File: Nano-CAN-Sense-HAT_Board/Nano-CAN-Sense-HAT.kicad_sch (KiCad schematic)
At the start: 33 parts, among them J1 Analog, J2 Digital, J3 Conn_02x04_Counter_Clockwise, J4 Conn_02x04_Counter_Clockwise, J5 Conn_01x05, J6 Conn_01x03, SW1 SW_Push, SW2 SW_Push, U1 LMC6484, U4 TCAN1044A

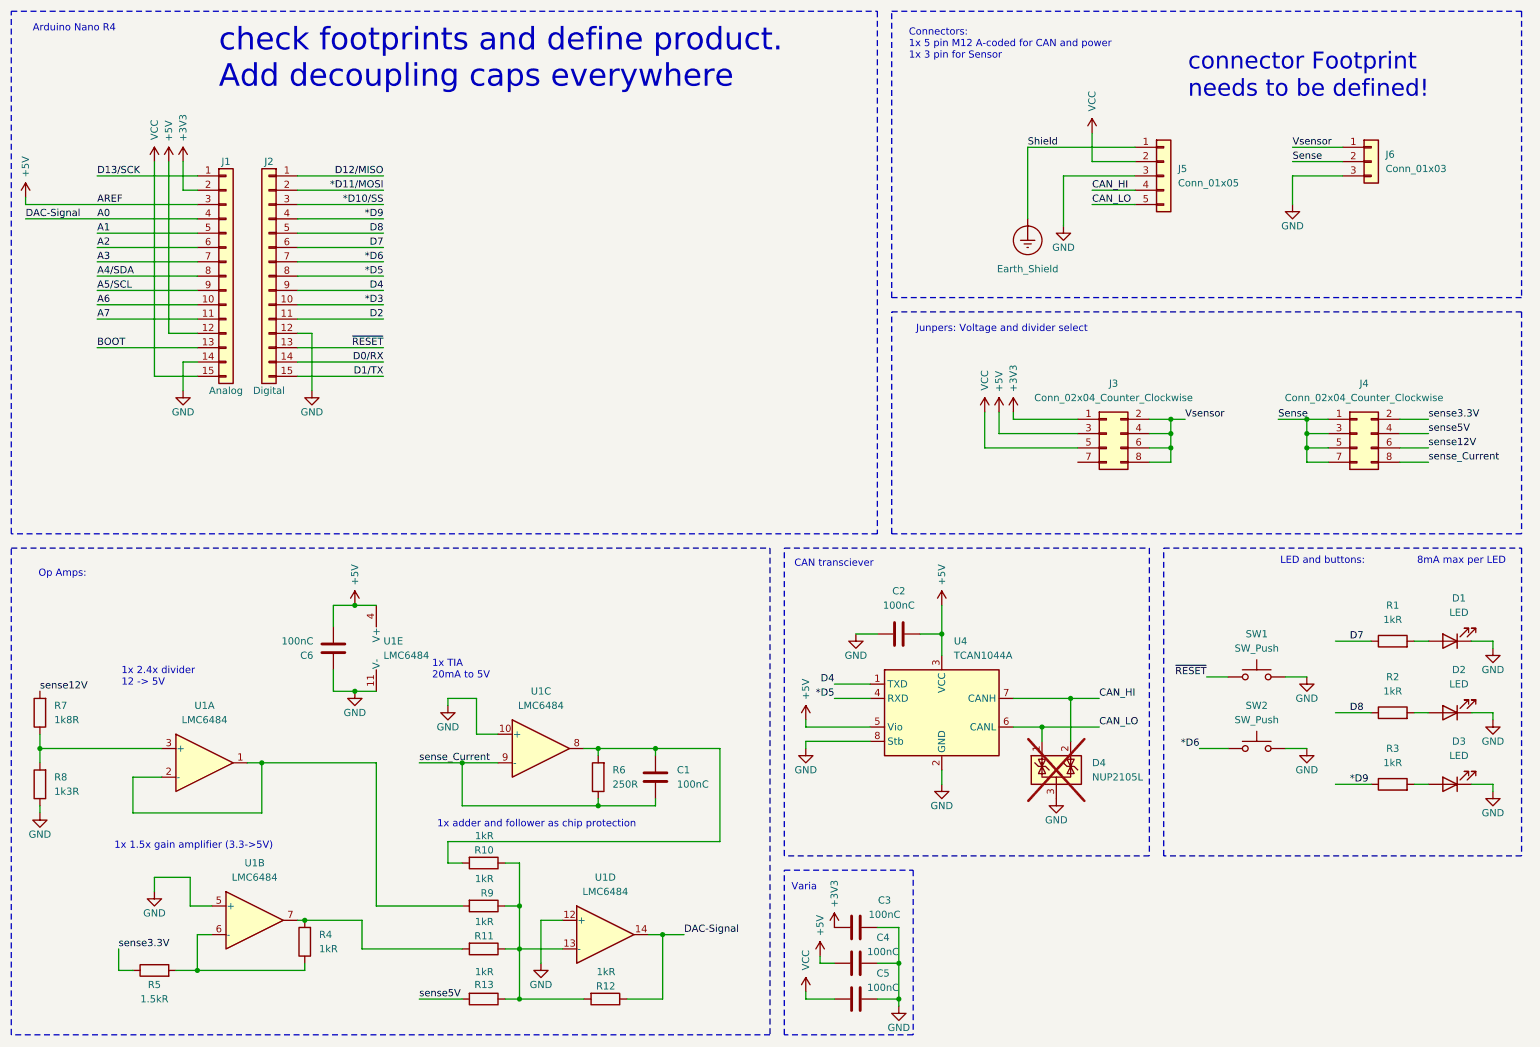
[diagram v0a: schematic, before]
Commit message: Improved Can for CAN-FD
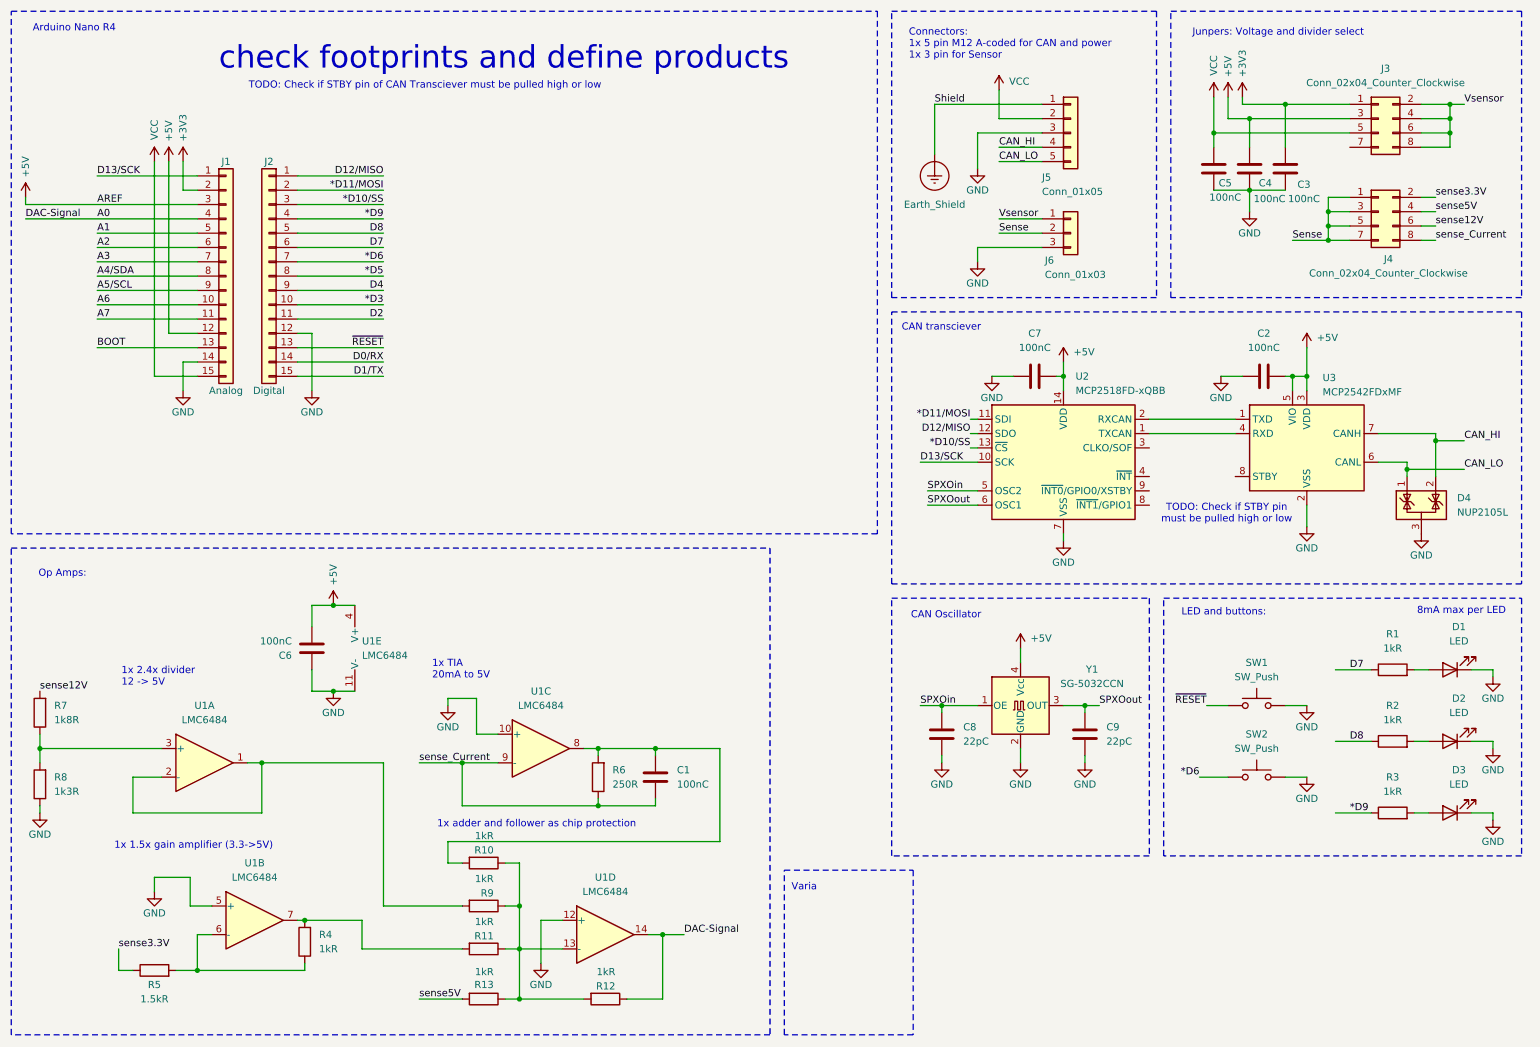
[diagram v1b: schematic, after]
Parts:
- removed U4: TCAN1044A, Package_SO:SOIC-8_3.9x4.9mm_P1.27mm, symbol Interface_CAN_LIN:TCAN330G
- added C7: 100nC, Capacitor_SMD:C_0603_1608Metric_Pad1.08x0.95mm_HandSolder, symbol Device:C
- added C8, C9: 22pC, Capacitor_SMD:C_0603_1608Metric_Pad1.08x0.95mm_HandSolder, symbol Device:C
- added U2: MCP2518FD-xQBB, Package_DFN_QFN:DFN-14-1EP_3x4.5mm_P0.65mm_EP1.65x4.25mm, symbol Interface_CAN_LIN:MCP2518FD-xQBB
- added U3: MCP2542FDxMF, Package_DFN_QFN:DFN-8-1EP_3x3mm_P0.65mm_EP1.55x2.4mm, symbol Interface_CAN_LIN:MCP2542FDxMF
- added Y1: SG-5032CCN, Oscillator:Oscillator_SMD_SeikoEpson_SG8002LB-4Pin_5.0x3.2mm, symbol Oscillator:SG-5032CCN
- D4: now fitted; now in the parts list
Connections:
- net *D10/SS: now also U2.13 (~{CS})
- net *D11/MOSI: now also U2.11 (SDI)
- net +5V: now also C7.2, U2.14 (VDD), U3.3 (VDD), U3.5 (VIO), Y1.4 (Vcc)
- net CAN_HI: now also U3.7 (CANH)
- net CAN_LO: now also U3.6 (CANL)
- net D12/MISO: now also U2.12 (SDO)
- net D13/SCK: now also U2.10 (SCK)
- net GND: now also C7.1, C8.1, C9.1, U2.15 (VSS), U2.7 (VSS), U3.2 (VSS), U3.9 (VSS), Y1.2 (GND)
- new net: U2.2 (RXCAN), U3.1 (TXD)
- new net: U2.1 (TXCAN), U3.4 (RXD)
- new net SPXOin: C8.2, U2.5 (OSC2), Y1.1 (OE)
- new net SPXOout: C9.2, U2.6 (OSC1), Y1.3 (OUT)
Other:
- note added: "CAN Oscillator"
- note added: "TODO: Check if STBY pin must be pulled high or low"
- note added: "TODO: Check if STBY pin of CAN Transciever must be pulled high or low"
- note added: "check footprints and define products"
- note removed: "check footprints and define product. Add decoupling caps everywhere"
- note removed: "connector Footprint needs to be defined!"
- moved on the sheet: C2, C6, D1, D2, D3, J3, J4, J5, J6, R1, R2, R3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

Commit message: Added Temp sensor SHT4x, rounded board edge
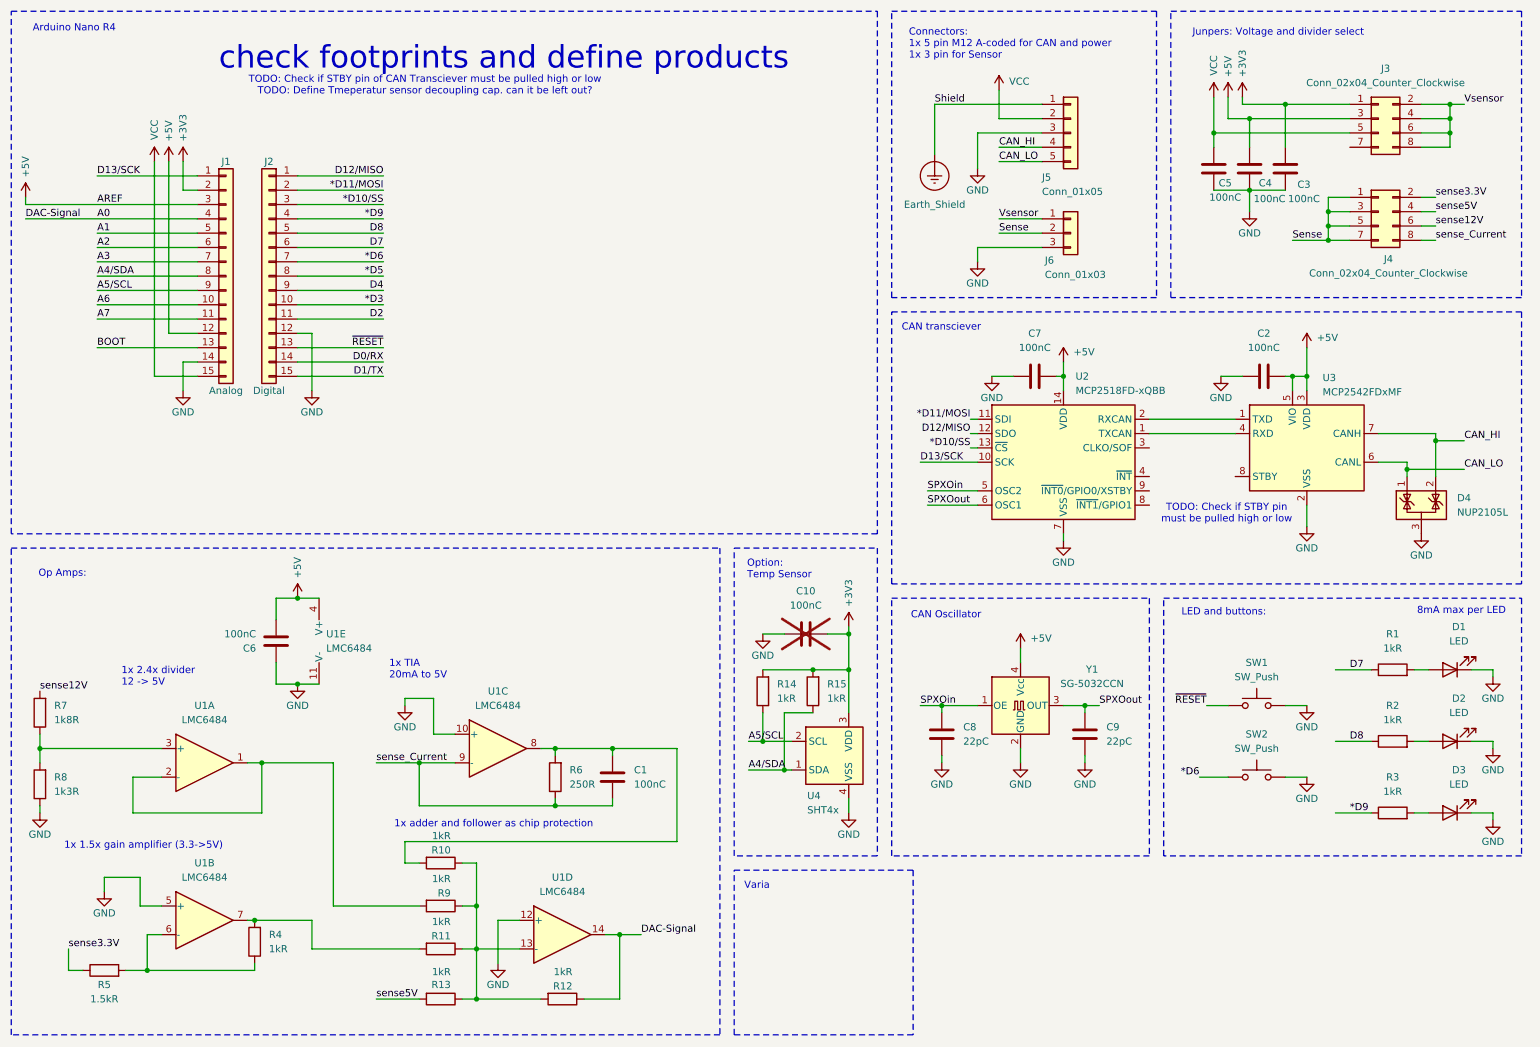
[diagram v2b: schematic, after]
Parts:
- added C10: 100nC, Capacitor_SMD:C_0603_1608Metric_Pad1.08x0.95mm_HandSolder, symbol Device:C
- added R14, R15: 1kR, Resistor_SMD:R_0603_1608Metric_Pad0.98x0.95mm_HandSolder, symbol Device:R
- added U4: SHT4x, Sensor_Humidity:Sensirion_DFN-4_1.5x1.5mm_P0.8mm_SHT4x_NoCentralPad, symbol Sensor_Humidity:SHT4x
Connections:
- net +3V3: now also C10.2, R14.2, R15.2, U4.3 (VDD)
- net A4/SDA: now also R15.1, U4.1 (SDA)
- net A5/SCL: now also R14.1, U4.2 (SCL)
- net GND: now also C10.1, U4.4 (VSS)
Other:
- note added: "Option: Temp Sensor"
- note added: "TODO: Check if STBY pin of CAN Transciever must be pulled high or low TODO: Define Tmeperatur sensor decoupling cap. can it be left out?"
- note removed: "TODO: Check if STBY pin of CAN Transciever must be pulled high or low"
- moved on the sheet: C1, C6, R10, R11, R12, R13, R4, R5, R6, R9, U1B, U1C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

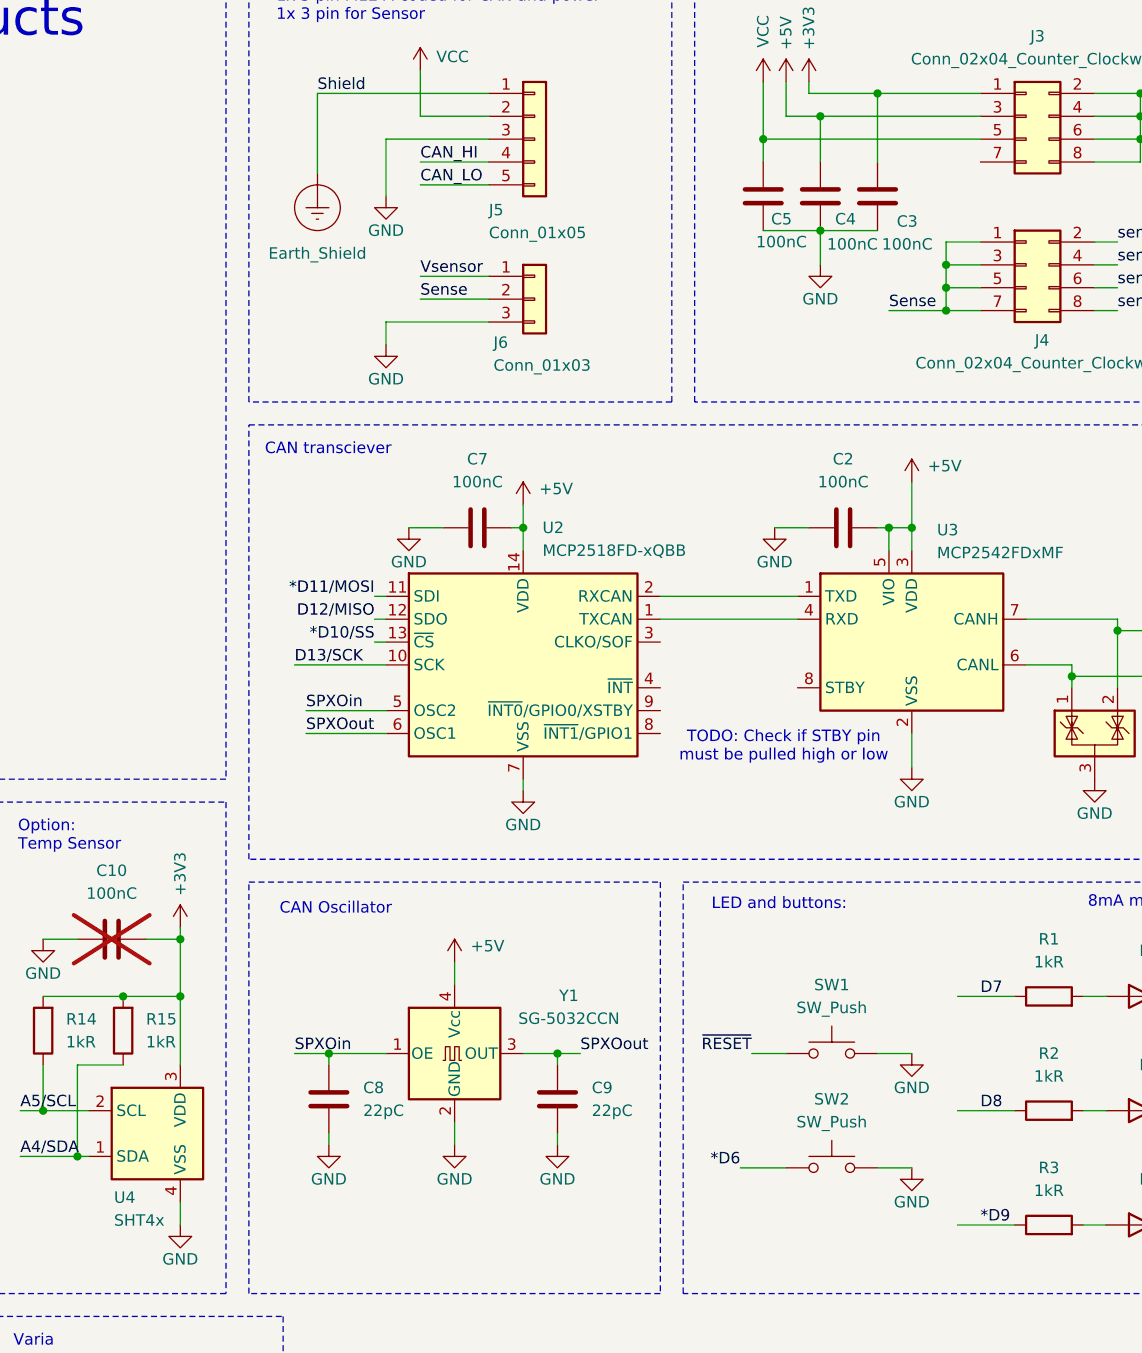
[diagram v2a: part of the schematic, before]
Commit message: Changed oscillator, improved GND layout
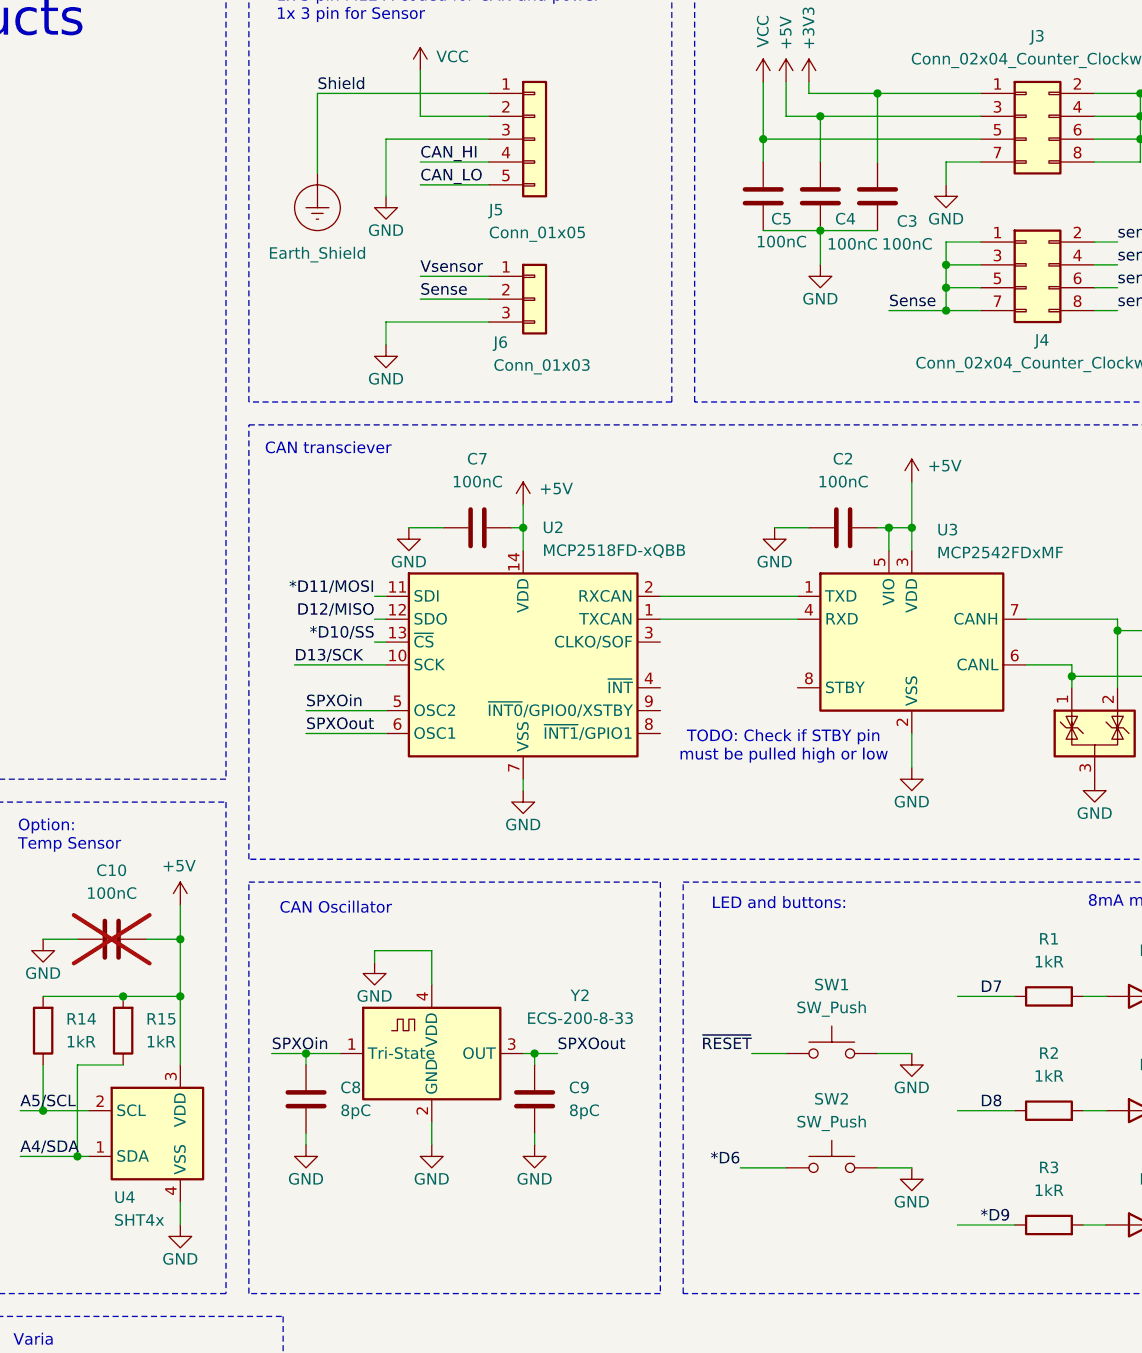
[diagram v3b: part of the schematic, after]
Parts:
- removed Y1: SG-5032CCN, Oscillator:Oscillator_SMD_SeikoEpson_SG8002LB-4Pin_5.0x3.2mm, symbol Oscillator:SG-5032CCN
- added Y2: ECS-200-8-33, Oscillator:Oscillator_SMD_ECS_2520MV-xxx-xx-4Pin_2.5x2.0mm, symbol Oscillator:ECS-2520MV-xxx-xx
- C8, C9: value 22pC -> 8pC
- U4: Comment (none) -> Need 5V tolderan Sensirion SHT41 or SHT30 model. SHTXXA-XX1B
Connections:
- net +3V3: no longer C10.2, R14.2, R15.2, U4.3 (VDD)
- net +5V: now also C10.2, R14.2, R15.2, U4.3 (VDD)
- net GND: now also J3.7 (Pin_7), Y2.2 (GND), Y2.4 (VDD)
- net SPXOin: now also Y2.1 (Tri-State)
- net SPXOout: now also Y2.3 (OUT)
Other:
- moved on the sheet: C8, C9
